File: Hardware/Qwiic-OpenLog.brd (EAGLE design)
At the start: 38.1 x 38.1 mm, 58 parts, among them J1 MICRO-SD, J10 GATORGATOR_MINI, J2 GATORGATOR_MINI, J3 GATORGATOR_MINI, J4 GATORGATOR_MINI, J5 ISP, J6 GATORGATOR_MINI, J7 GATORGATOR_MINI, J8 GATORGATOR_MINI, J9 GATORGATOR_MINI, Q1 16MHZ, U1 RV-1805, U2 ATMEGA328P

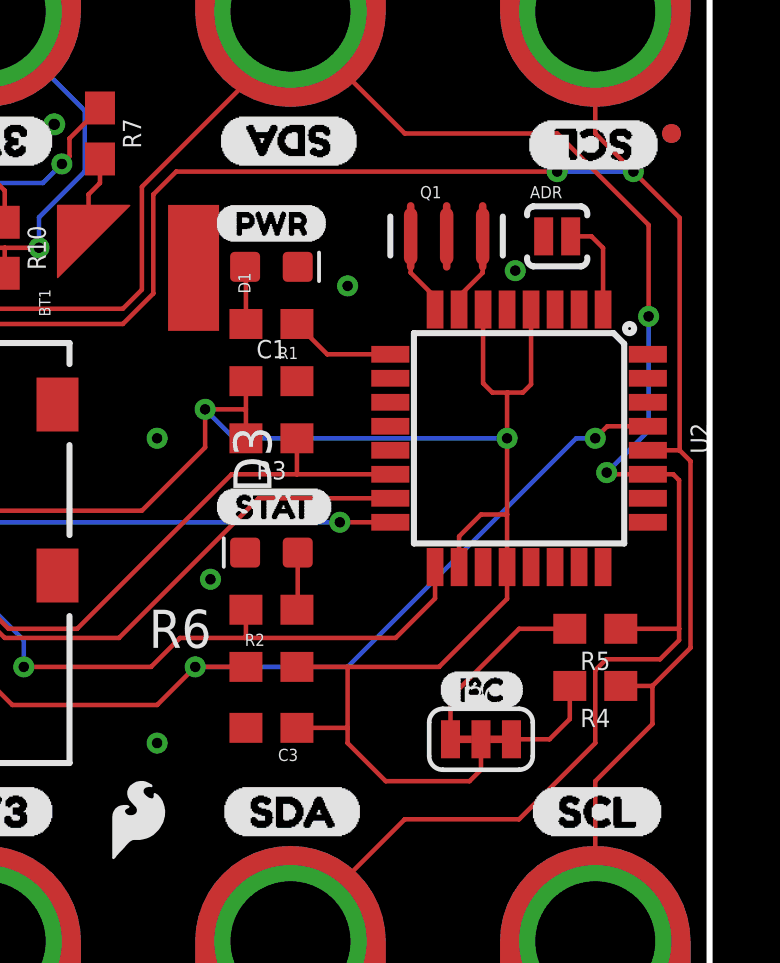
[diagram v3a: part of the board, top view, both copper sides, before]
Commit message: updating silk
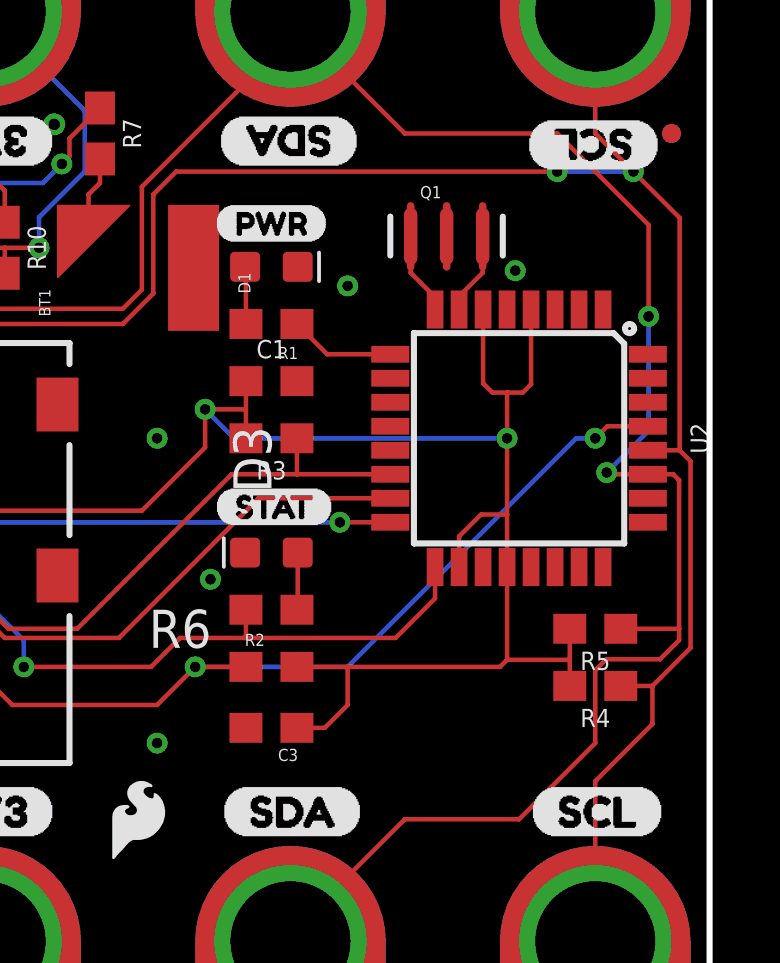
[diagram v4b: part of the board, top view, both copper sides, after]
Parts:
- removed ADR: (no value), SparkFun:SJ_2S-NO
- removed I2C: (no value), SparkFun-Jumpers:SMT-JUMPER_3_2-NC_TRACE_SILK
- removed U$8: (no value), Labels:I_SUPER2_C-()-03
- R4, R5: value 2.2k -> 10k
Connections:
- removed net N$5: I2C.1, R5.2
- removed net N$6: I2C.3, R4.2
- net 3.3V: now also R4.2, R5.2; no longer I2C.2
- net ADDR: no longer ADR.2
- net GND: no longer ADR.1
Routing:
- net N$5: track 6.32 -> 0.00 mm
- net N$6: track 3.33 -> 0.00 mm
- net ADDR: track 3.29 -> 0.00 mm
- net 3.3V: track 128.0 -> 126.1 mm
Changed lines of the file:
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@@
 <?xml version="1.0" encoding="utf-8"?>
 <!DOCTYPE eagle SYSTEM "eagle.dtd">
-<eagle version="9.3.1">
+<eagle version="9.1.0">
 <drawing>
 <settings>
@@
 <attribute name="VALUE" x="26.416" y="22.606" size="0.6096" layer="27" font="vector" ratio="20" align="top-center"/>
 </element>
-<element name="ADR" library="SparkFun" package="SJ_2S-NO" value="" x="33.02" y="27.051" smashed="yes">
-<attribute name="NAME" x="32.112" y="28.321" size="0.4064" layer="25"/>
-<attribute name="VALUE" x="32.112" y="25.4" size="0.4064" layer="27"/>
-</element>
-<element name="R4" library="SparkFun-Resistors" package="0603" value="2.2k" x="34.29" y="12.065" smashed="yes" rot="R180">
+<element name="R4" library="SparkFun-Resistors" package="0603" value="10k" x="34.29" y="12.065" smashed="yes" rot="R180">
 <attribute name="NAME" x="34.29" y="11.303" size="0.6096" layer="25" font="vector" ratio="20" rot="R180" align="bottom-center"/>
-<attribute name="PROD_ID" value="RES-08272" x="58.42" y="-36.195" size="1.778" layer="27" font="vector" ratio="15" rot="R180" display="off"/>
-<attribute name="VALUE" x="36.957" y="11.811" size="0.6096" layer="27" font="vector" ratio="20" rot="R180" align="top-center"/>
-</element>
-<element name="R5" library="SparkFun-Resistors" package="0603" value="2.2k" x="34.29" y="13.97" smashed="yes" rot="R180">
+<attribute name="PROD_ID" value="RES-00824" x="58.42" y="-36.195" size="1.778" layer="27" font="vector" ratio="15" rot="R180" display="off"/>
+<attribute name="VALUE" value="10k" x="36.957" y="11.811" size="0.6096" layer="27" font="vector" ratio="20" rot="R180" align="top-center"/>
+</element>
+<element name="R5" library="SparkFun-Resistors" package="0603" value="10k" x="34.29" y="13.97" smashed="yes" rot="R180">
 <attribute name="NAME" x="34.29" y="13.208" size="0.6096" layer="25" font="vector" ratio="20" rot="R180" align="bottom-center"/>
-<attribute name="PROD_ID" value="RES-08272" x="64.77" y="-30.48" size="1.778" layer="27" font="vector" ratio="15" rot="R180" display="off"/>
-<attribute name="VALUE" x="34.417" y="12.7" size="0.6096" layer="27" font="vector" ratio="20" rot="R180" align="top-center"/>
-</element>
-<element name="I2C" library="SparkFun-Jumpers" package="SMT-JUMPER_3_2-NC_TRACE_SILK" value="" x="30.48" y="10.287" smashed="yes">
-<attribute name="NAME" x="30.48" y="11.43" size="0.6096" layer="25" font="vector" ratio="20" align="bottom-center"/>
-<attribute name="VALUE" x="30.48" y="9.144" size="0.6096" layer="27" font="vector" ratio="20" align="top-center"/>
+<attribute name="PROD_ID" value="RES-00824" x="64.77" y="-30.48" size="1.778" layer="27" font="vector" ratio="15" rot="R180" display="off"/>
+<attribute name="VALUE" value="10k" x="34.417" y="12.7" size="0.6096" layer="27" font="vector" ratio="20" rot="R180" align="top-center"/>
 </element>
 <element name="J5" library="SparkFun-Connectors" package="2X3_TEST_POINTS" value="ISP" x="10.795" y="16.764" smashed="yes" rot="MR270">
@@
 <attribute name="VALUE" x="31.369" y="20.32" size="0.6096" layer="27" font="vector" ratio="20" rot="R270" align="bottom-center"/>
 </element>
-<element name="U$8" library="Labels" package="I_SUPER2_C-()-03" value="" x="29.083" y="11.938" smashed="yes"/>
 <element name="U$9" library="Labels" package="PWR-()-03" value="" x="21.6154" y="27.4828" smashed="yes"/>
 <element name="U$17" library="buzzard_labels (13)" package="STAT0" value="" x="21.59" y="18.034" smashed="yes"/>
@@
 </polygon>
 <contactref element="C1" pad="2"/>
-<contactref element="ADR" pad="1"/>
 <contactref element="J5" pad="6"/>
 <contactref element="U2" pad="3"/>
@@
 <contactref element="R2" pad="2"/>
 <contactref element="C1" pad="1"/>
-<contactref element="I2C" pad="2"/>
 <contactref element="J5" pad="2"/>
 <contactref element="U2" pad="6"/>
@@
 <wire x1="31.35" y1="17.78" x2="31.35" y2="20.32" width="0.1524" layer="1"/>
 <wire x1="31.369" y1="21.844" x2="31.35" y2="21.825" width="0.1524" layer="1"/>
-<wire x1="31.35" y1="16.0274" x2="31.35" y2="14.967" width="0.1524" layer="1"/>
-<wire x1="29.083" y1="12.7" x2="31.35" y2="14.967" width="0.1524" layer="1"/>
 <wire x1="24.345" y1="12.7" x2="26.035" y2="12.7" width="0.1524" layer="1"/>
-<wire x1="26.035" y1="12.7" x2="29.083" y2="12.7" width="0.1524" layer="1"/>
 <wire x1="5.864" y1="17.855" x2="5.939" y2="17.78" width="0.1524" layer="1"/>
 <wire x1="5.939" y1="17.78" x2="8.001" y2="17.78" width="0.1524" layer="1"/>
@@
 <wire x1="8.001" y1="17.78" x2="9.525" y2="19.304" width="0.1524" layer="16"/>
 <contactref element="J4" pad="P$2"/>
-<wire x1="26.035" y1="10.16" x2="27.305" y2="8.89" width="0.1524" layer="1"/>
-<wire x1="30.099" y1="8.89" x2="30.48" y2="9.271" width="0.1524" layer="1"/>
-<wire x1="30.48" y1="9.271" x2="30.48" y2="10.287" width="0.1524" layer="1"/>
-<wire x1="26.035" y1="12.7" x2="26.035" y2="10.668" width="0.1524" layer="1"/>
-<wire x1="26.035" y1="10.668" x2="26.035" y2="10.16" width="0.1524" layer="1"/>
-<wire x1="27.305" y1="8.89" x2="30.099" y2="8.89" width="0.1524" layer="1"/>
-<wire x1="24.345" y1="10.668" x2="26.035" y2="10.668" width="0.1524" layer="1"/>
 <wire x1="29.75" y1="16.0274" x2="29.75" y2="17.05" width="0.1524" layer="1"/>
 <wire x1="29.75" y1="17.05" x2="30.48" y2="17.78" width="0.1524" layer="1"/>
@@
 <wire x1="17.272" y1="29.21" x2="17.272" y2="31.242" width="0.1524" layer="16"/>
 <wire x1="17.272" y1="31.242" x2="13.97" y2="34.544" width="0.1524" layer="16"/>
+<contactref element="R4" pad="2"/>
+<contactref element="R5" pad="2"/>
+<wire x1="24.345" y1="10.668" x2="25.273" y2="10.668" width="0.1524" layer="1"/>
+<wire x1="25.273" y1="10.668" x2="26.035" y2="11.43" width="0.1524" layer="1"/>
+<wire x1="26.035" y1="11.43" x2="26.035" y2="12.7" width="0.1524" layer="1"/>
+<wire x1="33.44" y1="13.97" x2="33.44" y2="12.954" width="0.1524" layer="1"/>
+<wire x1="33.44" y1="12.954" x2="33.44" y2="12.065" width="0.1524" layer="1"/>
+<wire x1="31.35" y1="12.935" x2="31.115" y2="12.7" width="0.1524" layer="1"/>
+<wire x1="31.35" y1="16.0274" x2="31.35" y2="12.935" width="0.1524" layer="1"/>
+<wire x1="31.115" y1="12.7" x2="26.035" y2="12.7" width="0.1524" layer="1"/>
+<wire x1="31.35" y1="12.935" x2="33.421" y2="12.935" width="0.1524" layer="1"/>
+<wire x1="33.421" y1="12.935" x2="33.44" y2="12.954" width="0.1524" layer="1"/>
 <wire x1="22.2504" y1="20.32" x2="22.645" y2="20.32" width="0" layer="19" extent="1-16"/>
 <wire x1="21.285203125" y1="21.2852" x2="21.2852" y2="21.2852" width="0" layer="19" extent="1-16"/>
@@
 </signal>
 <signal name="ADDR">
-<contactref element="ADR" pad="2"/>
 <contactref element="U2" pad="1"/>
-<wire x1="34.55" y1="24.6126" x2="34.55" y2="26.664" width="0.1524" layer="1"/>
-<wire x1="34.163" y1="27.051" x2="33.47" y2="27.051" width="0.1524" layer="1"/>
-<wire x1="34.55" y1="26.664" x2="34.163" y2="27.051" width="0.1524" layer="1"/>
-</signal>
-<signal name="N$5">
-<contactref element="R5" pad="2"/>
-<contactref element="I2C" pad="1"/>
-<wire x1="29.464" y1="10.287" x2="29.464" y2="11.684" width="0.1524" layer="1"/>
-<wire x1="29.464" y1="11.684" x2="31.75" y2="13.97" width="0.1524" layer="1"/>
-<wire x1="31.75" y1="13.97" x2="33.44" y2="13.97" width="0.1524" layer="1"/>
-</signal>
-<signal name="N$6">
-<contactref element="R4" pad="2"/>
-<contactref element="I2C" pad="3"/>
-<wire x1="33.44" y1="12.065" x2="33.44" y2="10.961" width="0.1524" layer="1"/>
-<wire x1="33.44" y1="10.961" x2="32.766" y2="10.287" width="0.1524" layer="1"/>
-<wire x1="32.766" y1="10.287" x2="31.496" y2="10.287" width="0.1524" layer="1"/>
 </signal>
 <signal name="!INT">

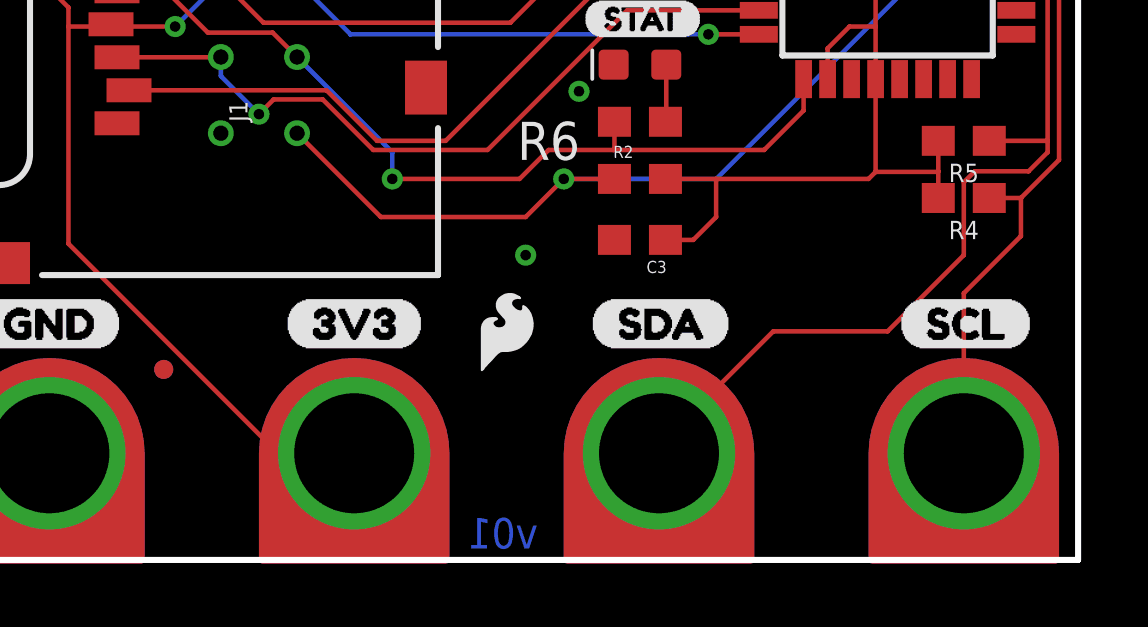
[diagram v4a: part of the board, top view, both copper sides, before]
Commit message: adding protection circuitry
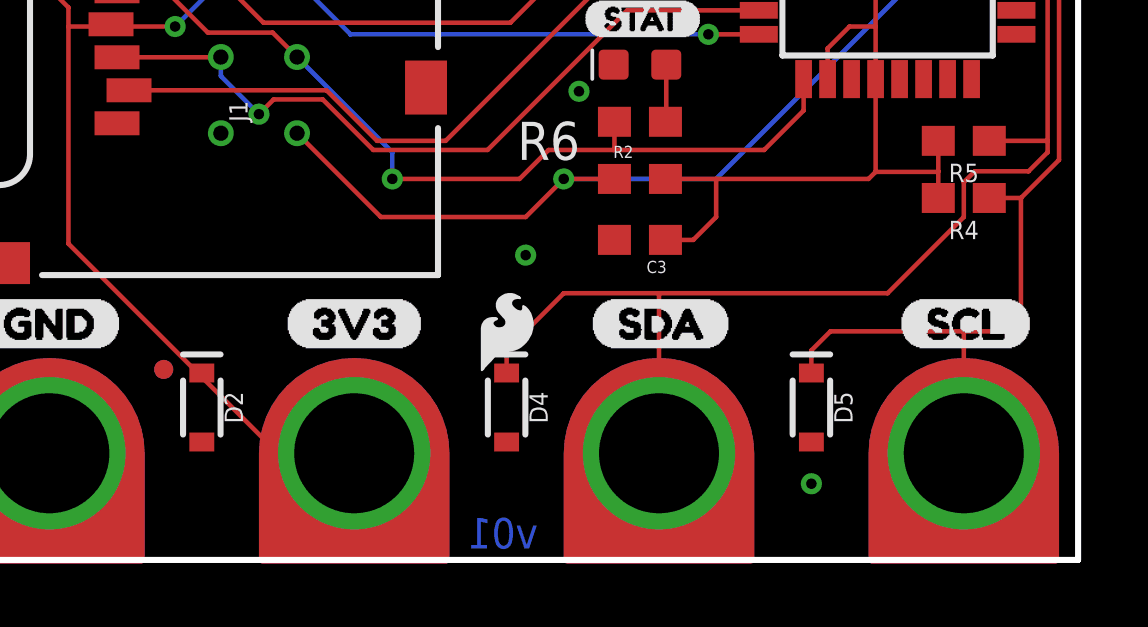
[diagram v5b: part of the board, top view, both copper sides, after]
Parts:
- added D2, D4, D5: 3.6V, SparkFun-DiscreteSemi:SOD-323
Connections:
- net 3.3V: now also D2.C
- net GND: now also D2.A, D4.A, D5.A
- net SCL: now also D5.C
- net SDA: now also D4.C
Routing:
- net SDA: track 74.4 -> 83.5 mm
- net SCL: track 68.1 -> 74.9 mm
- net GND: vias 10 -> 11
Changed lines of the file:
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@@
 <?xml version="1.0" encoding="utf-8"?>
 <!DOCTYPE eagle SYSTEM "eagle.dtd">
-<eagle version="9.1.0">
+<eagle version="9.3.1">
 <drawing>
 <settings>
@@
 <element name="U$16" library="buzzard_labels" package="SDA1" value="" x="26.416" y="7.874" smashed="yes" rot="MR0"/>
 <element name="U$18" library="buzzard_labels" package="SCL2" value="" x="36.449" y="7.874" smashed="yes" rot="MR0"/>
+<element name="D2" library="SparkFun-DiscreteSemi" package="SOD-323" value="3.6V" x="8.89" y="5.08" smashed="yes" rot="R270">
+<attribute name="NAME" x="9.652" y="5.08" size="0.6096" layer="25" font="vector" ratio="20" rot="R270" align="bottom-center"/>
+<attribute name="PROD_ID" value="DIO-08199" x="8.89" y="5.08" size="1.778" layer="27" rot="R270" display="off"/>
+<attribute name="VALUE" x="8.128" y="5.08" size="0.6096" layer="27" font="vector" ratio="20" rot="R270" align="top-center"/>
+</element>
+<element name="D4" library="SparkFun-DiscreteSemi" package="SOD-323" value="3.6V" x="19.05" y="5.08" smashed="yes" rot="R270">
+<attribute name="NAME" x="19.812" y="5.08" size="0.6096" layer="25" font="vector" ratio="20" rot="R270" align="bottom-center"/>
+<attribute name="PROD_ID" value="DIO-08199" x="19.05" y="5.08" size="1.778" layer="27" rot="R270" display="off"/>
+<attribute name="VALUE" x="18.288" y="5.08" size="0.6096" layer="27" font="vector" ratio="20" rot="R270" align="top-center"/>
+</element>
+<element name="D5" library="SparkFun-DiscreteSemi" package="SOD-323" value="3.6V" x="29.21" y="5.08" smashed="yes" rot="R270">
+<attribute name="NAME" x="29.972" y="5.08" size="0.6096" layer="25" font="vector" ratio="20" rot="R270" align="bottom-center"/>
+<attribute name="PROD_ID" value="DIO-08199" x="29.21" y="5.08" size="1.778" layer="27" rot="R270" display="off"/>
+<attribute name="VALUE" x="28.448" y="5.08" size="0.6096" layer="27" font="vector" ratio="20" rot="R270" align="top-center"/>
+</element>
 </elements>
 <signals>
@@
 <wire x1="7.1414" y1="27.2756" x2="6.82" y2="27.597" width="0.1524" layer="1"/>
 <contactref element="BT1" pad="-"/>
+<contactref element="D5" pad="A"/>
+<contactref element="D4" pad="A"/>
+<contactref element="D2" pad="A"/>
+<via x="29.21" y="2.54" extent="1-16" drill="0.35"/>
 </signal>
 <signal name="SCK">
@@
 <wire x1="31.35" y1="12.935" x2="33.421" y2="12.935" width="0.1524" layer="1"/>
 <wire x1="33.421" y1="12.935" x2="33.44" y2="12.954" width="0.1524" layer="1"/>
+<contactref element="D2" pad="C"/>
 <wire x1="22.2504" y1="20.32" x2="22.645" y2="20.32" width="0" layer="19" extent="1-16"/>
 <wire x1="21.285203125" y1="21.2852" x2="21.2852" y2="21.2852" width="0" layer="19" extent="1-16"/>
+<wire x1="8.89" y1="6.23" x2="11.43" y2="3.556" width="0" layer="19" extent="1-1"/>
 </signal>
 <signal name="SCL">
@@
 <wire x1="37.103" y1="27.667" x2="35.56" y2="29.21" width="0.1524" layer="1"/>
 <wire x1="35.56" y1="29.21" x2="34.29" y2="30.48" width="0.1524" layer="1"/>
-<wire x1="36.195" y1="12.065" x2="36.195" y2="10.795" width="0.1524" layer="1"/>
-<wire x1="36.195" y1="10.795" x2="34.29" y2="8.89" width="0.1524" layer="1"/>
-<wire x1="34.29" y1="8.89" x2="34.29" y2="3.556" width="0.1524" layer="1"/>
 <contactref element="U1" pad="4"/>
 <wire x1="8.42" y1="25.57" x2="8.42" y2="24.6" width="0.1524" layer="1"/>
@@
 <wire x1="33.02" y1="29.21" x2="35.56" y2="29.21" width="0.1524" layer="16"/>
 <via x="35.56" y="29.21" extent="1-16" drill="0.35"/>
+<contactref element="D5" pad="C"/>
+<wire x1="29.21" y1="6.23" x2="29.21" y2="6.985" width="0.1524" layer="1"/>
+<wire x1="29.21" y1="6.985" x2="29.845" y2="7.62" width="0.1524" layer="1"/>
+<wire x1="29.845" y1="7.62" x2="34.29" y2="7.62" width="0.1524" layer="1"/>
+<wire x1="34.29" y1="7.62" x2="35.56" y2="7.62" width="0.1524" layer="1"/>
+<wire x1="35.56" y1="7.62" x2="36.195" y2="8.255" width="0.1524" layer="1"/>
+<wire x1="36.195" y1="8.255" x2="36.195" y2="12.065" width="0.1524" layer="1"/>
+<wire x1="34.29" y1="3.556" x2="34.29" y2="7.62" width="0.1524" layer="1"/>
 </signal>
 <signal name="SDA">
@@
 <wire x1="34.6557125" y1="12.954" x2="34.29" y2="12.5882875" width="0.1524" layer="1"/>
 <wire x1="36.449" y1="12.954" x2="34.6557125" y2="12.954" width="0.1524" layer="1"/>
-<wire x1="34.29" y1="12.5882875" x2="34.29" y2="10.16" width="0.1524" layer="1"/>
-<wire x1="34.29" y1="10.16" x2="31.75" y2="7.62" width="0.1524" layer="1"/>
-<wire x1="31.75" y1="7.62" x2="27.94" y2="7.62" width="0.1524" layer="1"/>
-<wire x1="27.94" y1="7.62" x2="24.13" y2="3.81" width="0.1524" layer="1"/>
+<wire x1="34.29" y1="12.5882875" x2="34.29" y2="11.43" width="0.1524" layer="1"/>
+<wire x1="34.29" y1="11.43" x2="31.75" y2="8.89" width="0.1524" layer="1"/>
 <wire x1="24.13" y1="3.81" x2="24.13" y2="3.556" width="0.1524" layer="1"/>
 <wire x1="37.084" y1="18.923" x2="37.084" y2="13.97" width="0.1524" layer="1"/>
@@
 <wire x1="24.13" y1="33.655" x2="24.13" y2="34.29" width="0.1524" layer="1"/>
 <wire x1="19.177" y1="28.702" x2="24.13" y2="33.655" width="0.1524" layer="1"/>
+<contactref element="D4" pad="C"/>
+<wire x1="19.05" y1="6.23" x2="19.05" y2="6.985" width="0.1524" layer="1"/>
+<wire x1="20.955" y1="8.89" x2="19.05" y2="6.985" width="0.1524" layer="1"/>
+<wire x1="31.75" y1="8.89" x2="24.13" y2="8.89" width="0.1524" layer="1"/>
+<wire x1="24.13" y1="8.89" x2="20.955" y2="8.89" width="0.1524" layer="1"/>
+<wire x1="24.13" y1="3.556" x2="24.13" y2="8.89" width="0.1524" layer="1"/>
 </signal>
 <signal name="ADDR">
